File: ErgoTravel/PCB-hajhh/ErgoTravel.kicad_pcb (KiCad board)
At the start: 2 copper layers, 137.9 x 92.7 mm, 43 parts, among them J1 , J10 AudioJack3_Ground, J11 AudioJack3_Ground, J2 , J3 , J4 , J5 , J6 , J7 , J8 , SW1 , SW10 , SW11 , SW12 , SW13 , SW14 , SW15 , SW16 , SW17 , SW18 , SW19 , SW2 , SW20 , SW21 , SW22 , SW23 , SW24 , SW25 , SW26 , SW27 , SW28 , SW29 RST, SW3 , SW30 , SW31 , SW4 , SW5 , SW6 , SW7 , SW8 , SW9 , U1 Promicro

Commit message: update 13:33 24/01/2021
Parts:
- removed the J10 at (200.5, 52.5)
- added D1: , fruitkt:DIODE, F.Cu at (92.7, 64.0)
- added D10: , fruitkt:DIODE, F.Cu at (114.0, 78.5)
- added D11: , fruitkt:DIODE, F.Cu at (152.4, 73.7)
- added D12: , fruitkt:DIODE, F.Cu at (168.9, 74.2)
- added D13: , fruitkt:DIODE, F.Cu at (171.4, 74.2)
- added D14: , fruitkt:DIODE, F.Cu at (190.5, 85.7)
- added D15: , fruitkt:DIODE, F.Cu at (92.7, 102.2)
- added D16: , fruitkt:DIODE, F.Cu at (111.8, 99.6)
- added D17: , fruitkt:DIODE, F.Cu at (130.6, 95.8)
- added D18: , fruitkt:DIODE, F.Cu at (133.4, 95.8)
- added D19: , fruitkt:DIODE, F.Cu at (152.4, 97.8)
- added D2: , fruitkt:DIODE, F.Cu at (111.8, 61.0)
- added D20: , fruitkt:DIODE, F.Cu at (171.4, 99.8)
- added D21: , fruitkt:DIODE, F.Cu at (189.5, 104.1)
- added D22: , fruitkt:DIODE, F.Cu at (92.5, 120.9)
- added D23: , fruitkt:DIODE, F.Cu at (111.5, 117.1)
- added D24: , fruitkt:DIODE, F.Cu at (114.3, 116.8)
- added D25: , fruitkt:DIODE, F.Cu at (133.1, 114.0)
- added D26: , fruitkt:DIODE, F.Cu at (158.1, 116.2)
- added D27: , fruitkt:DIODE, F.Cu at (176.8, 124.5)
- added D28: , fruitkt:DIODE, F.Cu at (179.6, 119.6)
- added D3: , fruitkt:DIODE, F.Cu at (114.3, 60.7)
- added D4: , fruitkt:DIODE, F.Cu at (152.7, 62.0)
- added D5: , fruitkt:DIODE, F.Cu at (168.7, 61.7)
- added D6: , fruitkt:DIODE, F.Cu at (171.2, 61.7)
- added D7: , fruitkt:DIODE, F.Cu at (190.5, 66.3)
- added D8: , fruitkt:DIODE, F.Cu at (93.0, 83.1)
- added D9: , fruitkt:DIODE, F.Cu at (111.5, 78.5)
- added J12: OLED, fruitkt:OLED-0.91, F.Cu at (198.8, 93.4)
- added J13: , fruitkt:USB-C-16pin-hight, F.Cu at (205.8, 52.5)
- added J14: , fruitkt:USB-C-16pin-hight, B.Cu at (205.8, 52.5)
- added J15: , Connector_PinHeader_2.54mm:PinHeader_1x02_P2.54mm_Vertical, F.Cu at (183.1, 114.6)
- added J16: AVR-ISP-6, Connector_PinHeader_2.54mm:PinHeader_2x03_P2.54mm_Vertical, F.Cu at (133.0, 89.0)
- added J3: AudioJack4, Connector_Audio:Jack_3.5mm_PJ320D_Horizontal, F.Cu at (200.5, 52.5)
- added J4: AudioJack4, Connector_Audio:Jack_3.5mm_PJ320D_Horizontal, B.Cu at (200.5, 52.5)
- added JP1: , footprints:Jump, F.Cu at (194.9, 96.3)
- added JP10: , Jumper:SolderJumper-3_P1.3mm_Bridged12_Pad1.0x1.5mm_NumberLabels, F.Cu at (191.5, 53.9)
- added JP2: , footprints:Jump, F.Cu at (197.5, 96.3)
- added JP3: , footprints:Jump, F.Cu at (200.0, 96.3)
- added JP4: , footprints:Jump, F.Cu at (202.6, 96.3)
- added JP5: , footprints:Jump, B.Cu at (194.9, 96.3)
- added JP6: , footprints:Jump, B.Cu at (197.5, 96.3)
- added JP7: , footprints:Jump, B.Cu at (200.0, 96.3)
- added JP8: , footprints:Jump, B.Cu at (202.6, 96.3)
- added JP9: , Jumper:SolderJumper-3_P1.3mm_Bridged12_Pad1.0x1.5mm_NumberLabels, F.Cu at (191.5, 51.3)
- added LED1: , footprints:SK6812mini-e-R2L, F.Cu at (198.8, 66.3)
- added LED10: , footprints:SK6812mini-e-L2R, F.Cu at (160.6, 78.3)
- added LED11: , footprints:SK6812mini-e-L2R, F.Cu at (141.6, 75.9)
- added LED12: , footprints:SK6812mini-e-L2R, F.Cu at (122.5, 78.3)
- added LED13: , footprints:SK6812mini-e-L2R, F.Cu at (103.5, 80.7)
- added LED14: , footprints:SK6812mini-e-L2R, F.Cu at (84.4, 83.1)
- added LED15: , footprints:SK6812mini-e-R2L, F.Cu at (179.7, 99.7)
- added LED16: , footprints:SK6812mini-e-R2L, F.Cu at (160.6, 97.3)
- added LED17: , footprints:SK6812mini-e-R2L, F.Cu at (141.6, 95.0)
- added LED18: , footprints:SK6812mini-e-R2L, F.Cu at (122.5, 97.3)
- added LED19: , footprints:SK6812mini-e-R2L, F.Cu at (103.5, 99.7)
- added LED2: , footprints:SK6812mini-e-R2L, F.Cu at (179.7, 61.6)
- added LED20: , footprints:SK6812mini-e-R2L, F.Cu at (84.4, 102.1)
- added LED21: , footprints:SK6812mini-e-L2R, F.Cu at (84.4, 121.1)
- added LED22: , footprints:SK6812mini-e-L2R, F.Cu at (200.0, 109.7)
- added LED23: , footprints:SK6812mini-e-R2L, F.Cu at (195.2, 117.9)
- added LED24: , footprints:SK6812mini-e-L2R, F.Cu at (167.2, 118.4)
- added LED25: , footprints:SK6812mini-e-L2R, F.Cu at (141.6, 114.0)
- added LED26: , footprints:SK6812mini-e-L2R, F.Cu at (122.6, 116.4)
- added LED27: , footprints:SK6812mini-e-L2R, F.Cu at (103.5, 118.8)
- added LED28: , fruitkt:SK6812MINI-FLIP, F.Cu at (170.1, 68.8)
- added LED29: , fruitkt:SK6812MINI-FLIP, F.Cu at (170.2, 88.7)
- added LED3: , footprints:SK6812mini-e-R2L, F.Cu at (160.6, 59.2)
- added LED30: , fruitkt:SK6812MINI-FLIP, F.Cu at (170.2, 109.2)
- added LED31: , fruitkt:SK6812MINI-FLIP, F.Cu at (113.0, 109.2)
- added LED32: , fruitkt:SK6812MINI-FLIP, F.Cu at (113.0, 88.6)
- added LED33: , fruitkt:SK6812MINI-FLIP, F.Cu at (113.0, 69.1)
- added LED4: , footprints:SK6812mini-e-R2L, F.Cu at (141.7, 56.8)
- added LED5: , footprints:SK6812mini-e-R2L, F.Cu at (122.5, 59.1)
- added LED6: , footprints:SK6812mini-e-R2L, F.Cu at (103.5, 61.6)
- added LED7: , footprints:SK6812mini-e-R2L, F.Cu at (84.4, 63.9)
- added LED8: , footprints:SK6812mini-e-L2R, F.Cu at (198.7, 85.4)
- added LED9: , footprints:SK6812mini-e-L2R, F.Cu at (179.7, 80.7)
- added R1: 4K7, Resistor_SMD:R_0805_2012Metric, F.Cu at (186.4, 53.9)
- added R2: 4K7, Resistor_SMD:R_0805_2012Metric, F.Cu at (186.4, 51.2)
- J11: value AudioJack3_Ground -> (none); footprint Connector_Audio:Jack_3.5mm_PJ320D_Horizontal -> Connector_PinHeader_2.54mm:PinHeader_1x02_P2.54mm_Vertical; moved to F.Cu
- SW16: renamed from SW29; footprint Button_Switch_SMD:SW_SPST_TL3342 -> footprints:SW_TACT_ALPS_SKQGABE010
- SW8: renamed from SW30; footprint Button_Switch_SMD:SW_SPDT_PCM12 -> footprints:SW_SPDT_PCM12
- moved J11 80.6 mm to (120.0, 49.0)
- moved SW8 5.90 mm to (127.6, 49.3), turned to 0 degrees
- moved SW16 1.45 mm to (111.9, 51.2), turned to 10 degrees
- moved U1 0.25 mm to (141.6, 64.3)
- renumbered J8 to J10, J5 to J2, J2 to J5, J3 to J7, J7 to J8, J4 to J9, SW6 to SW10, SW10 to SW11, SW14 to SW12, SW18 to SW13, SW22 to SW14, SW27 to SW15, SW25 to SW17, SW31 to SW18, SW3 to SW19, SW5 to SW2, SW7 to SW20, SW11 to SW21, SW15 to SW22, SW19 to SW23, SW23 to SW24, SW28 to SW25, SW4 to SW26, SW8 to SW27, SW12 to SW28, SW16 to SW29, SW9 to SW3, SW20 to SW30, SW24 to SW31, SW13 to SW4, SW17 to SW5, SW21 to SW6, SW26 to SW7, SW2 to SW9
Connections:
- net Net-(SW29-Pad1) renamed RST
- net Net-(U1-PadB5) renamed backlight
- SW1 pad 1: Net-(SW1-Pad1) -> col0
- SW10 pad 1: Net-(SW6-Pad1) -> col1
- SW11 pad 1: Net-(SW10-Pad1) -> col2
- SW12 pad 1: Net-(SW14-Pad1) -> col3
- SW13 pad 1: Net-(SW18-Pad1) -> col4
- SW14 pad 1: Net-(SW22-Pad1) -> col5
- SW15 pad 1: Net-(SW27-Pad1) -> col6
- SW17 pad 1: Net-(D27-Pad2) (its old number) -> col6
- SW17 pad 2: Net-(SW25-Pad2) -> Net-(D21-Pad2)
- SW18 pad A: Net-(SW31-PadA) -> A
- SW18 pad B: Net-(SW31-PadB) -> B
- SW18 pad S1: Net-(SW31-PadS1) -> col6
- SW18 pad S2: Net-(SW31-PadS2) -> Net-(D21-Pad2)
- SW19 pad 1: Net-(SW3-Pad1) -> col0
- SW2 pad 1: Net-(SW5-Pad1) -> col1
- SW20 pad 1: Net-(SW7-Pad1) -> col1
- SW21 pad 1: Net-(SW11-Pad1) -> col2
- SW22 pad 1: Net-(SW15-Pad1) -> col3
- SW23 pad 1: Net-(SW19-Pad1) -> col4
- SW24 pad 1: Net-(SW23-Pad1) -> col5
- SW25 pad 1: Net-(SW25-Pad2) -> Net-(D21-Pad2)
- SW25 pad 2: Net-(D27-Pad2) (its old number) -> col6
- SW26 pad 1: Net-(SW4-Pad1) -> col0
- SW27 pad 1: Net-(SW8-Pad1) (its old number) -> col1
- SW28 pad 1: Net-(SW12-Pad1) -> col2
- SW29 pad 1: Net-(SW16-Pad1) -> col3
- SW3 pad 1: Net-(SW9-Pad1) -> col2
- SW30 pad 1: Net-(SW20-Pad1) -> col4
- SW31 pad 1: Net-(SW24-Pad1) -> col5
- SW4 pad 1: Net-(SW13-Pad1) -> col3
- SW5 pad 1: Net-(SW17-Pad1) -> col4
- SW6 pad 1: Net-(SW21-Pad1) -> col5
- SW7 pad 1: Net-(SW26-Pad1) -> col6
- SW8 pad 3: Net-(SW30-Pad3) -> Net-(J11-Pad1)
- SW9 pad 1: Net-(SW2-Pad1) -> col0
- U1 pad B1: Net-(U1-PadB1) -> col3
- U1 pad B2: Net-(U1-PadB2) -> col5
- U1 pad B3: Net-(U1-PadB3) -> col4
- U1 pad B4: Net-(U1-PadB4) -> row3
- U1 pad B6: Net-(U1-PadB6) -> col6
- U1 pad C6: Net-(U1-PadC6) -> row0
- U1 pad D0: Net-(U1-PadD0) -> scl
- U1 pad D1: Net-(U1-PadD1) -> sda
- U1 pad D2: Net-(U1-PadD2) -> rx
- U1 pad D3: Net-(U1-PadD3) -> led
- U1 pad D4: Net-(U1-PadD4) -> A
- U1 pad D7: Net-(U1-PadD7) -> row1
- U1 pad E6: Net-(U1-PadE6) -> row2
- U1 pad F4: Net-(U1-PadF4) -> B
- U1 pad F5: Net-(U1-PadF5) -> col0
- U1 pad F6: Net-(U1-PadF6) -> col1
- U1 pad F7: Net-(U1-PadF7) -> col2
- U1 pad VCC: Net-(U1-PadVCC) -> VCC
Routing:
- net VCC: track 0.00 -> 988.8 mm, vias 0 -> 20
- net GND: track 0.00 -> 528.7 mm, vias 0 -> 21
- net col6: track 0.00 -> 172.5 mm
- net col5: track 0.00 -> 168.0 mm
- net row3: track 0.00 -> 145.7 mm
- net col0: track 0.00 -> 143.1 mm
- net col4: track 0.00 -> 140.4 mm
- net row2: track 0.00 -> 131.7 mm
- net col1: track 0.00 -> 125.4 mm
- net row1: track 0.00 -> 122.5 mm, vias 0 -> 1
- net col3: track 0.00 -> 121.1 mm
- net row0: track 0.00 -> 113.5 mm
- net scl: track 0.00 -> 110.3 mm, vias 0 -> 1
- net sda: track 0.00 -> 105.2 mm, vias 0 -> 2
- net col2: track 0.00 -> 103.2 mm
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- added copper zone on B.Cu, net GND
- added copper zone on F.Cu, net GND
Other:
- net class Wires: trace_width 0.5 -> 0.4
- board text added: "Use ProMicro or nRFMicro"
- board text removed: "Extra Key"
- board text removed: "Install D28 for Extra Key"
- board text removed: "Use Pro Micro or BlueMicro"

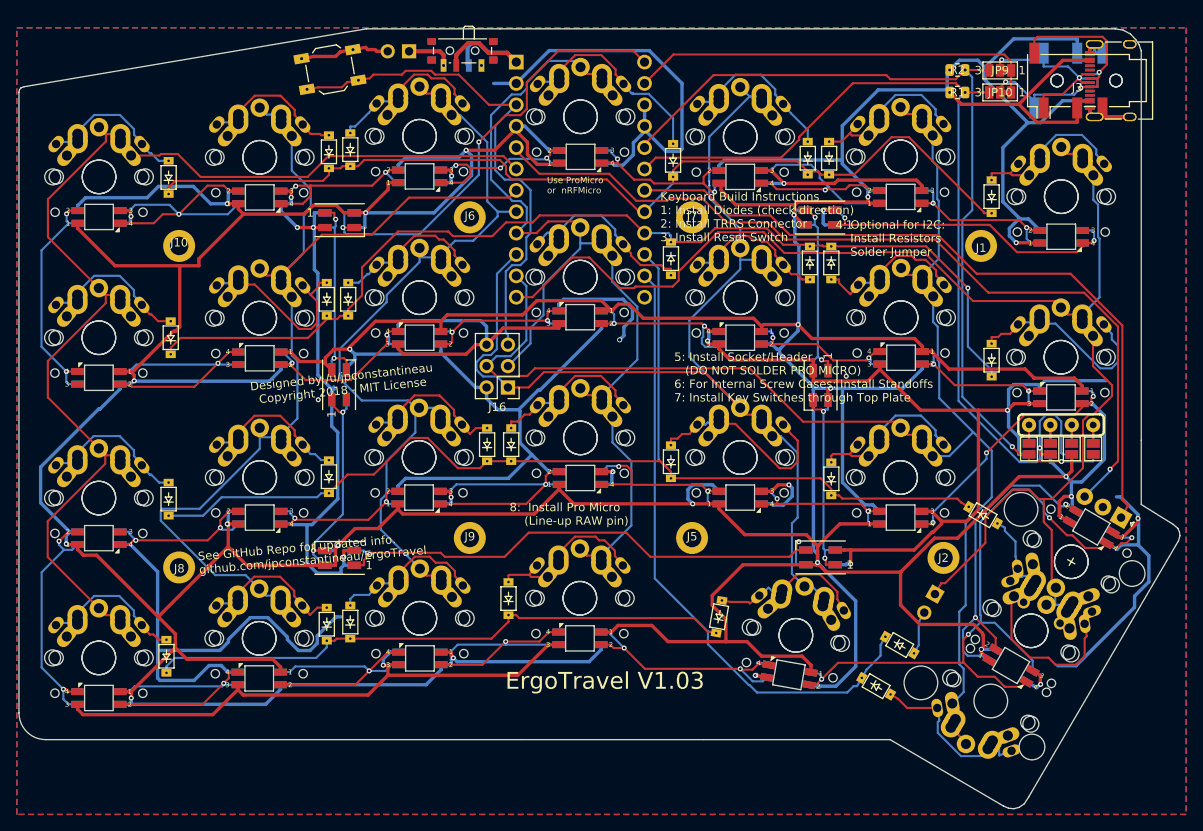
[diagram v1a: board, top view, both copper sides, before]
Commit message: add some keyboard
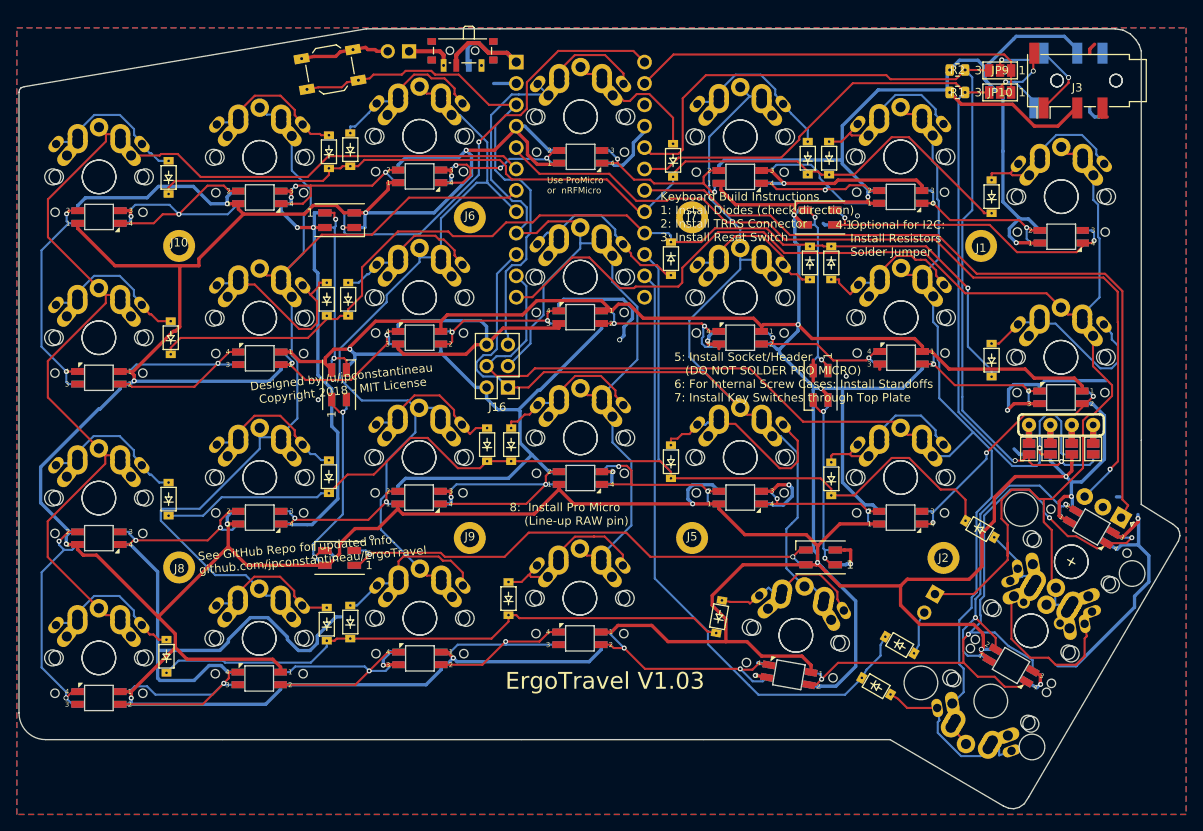
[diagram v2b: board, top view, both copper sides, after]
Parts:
- removed J13, J14: , fruitkt:USB-C-16pin-hight
- moved D21 1.69 mm to (189.1, 105.8)
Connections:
- J1 pad 1: Net-(J1-Pad1) -> GND
- J10 pad 1: Net-(J10-Pad1) -> GND
- J2 pad 1: Net-(J2-Pad1) -> GND
- J5 pad 1: Net-(J5-Pad1) -> GND
- J6 pad 1: Net-(J6-Pad1) -> GND
- J7 pad 1: Net-(J7-Pad1) -> GND
- J8 pad 1: Net-(J8-Pad1) -> GND
- J9 pad 1: Net-(J9-Pad1) -> GND
- SW4 pad 1: col3 -> Net-(D4-Pad2)
- SW4 pad 2: Net-(D4-Pad2) -> col3
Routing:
- net GND: track 528.7 -> 318.9 mm
- net VCC: track 988.8 -> 963.3 mm
- net 1: track 35.6 -> 11.6 mm, vias 3 -> 2
- net 2: track 26.4 -> 16.1 mm
- net Net-(D4-Pad2): track 26.9 -> 18.0 mm
- net sda: track 105.2 -> 111.4 mm
- net row2: track 131.7 -> 137.2 mm
- net col6: track 172.5 -> 177.6 mm
- net col3: track 121.1 -> 125.9 mm
- net Net-(LED30-PadI): track 64.7 -> 61.2 mm
- net B: track 102.6 -> 105.0 mm
- net A: track 86.8 -> 89.2 mm
- net Net-(LED31-PadI): track 25.6 -> 27.4 mm
- net Net-(D21-Pad2): track 38.7 -> 37.2 mm
- net scl: track 110.3 -> 111.7 mm
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
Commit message: cap nhat 12:00 18/03/2021
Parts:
- moved D23 0.47 mm to (111.9, 116.9)
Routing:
- net GND: track 318.9 -> 256.9 mm, vias 21 -> 20
- net VCC: track 963.3 -> 971.6 mm
- net row1: track 122.5 -> 127.2 mm
- net row3: track 145.4 -> 149.0 mm
- net Net-(LED26-PadI): track 30.6 -> 32.6 mm
- net Net-(LED24-PadI): track 29.0 -> 28.0 mm
- net Net-(D7-Pad2): track 20.4 -> 19.5 mm
- net Net-(LED30-PadI): track 61.2 -> 62.0 mm
- net Net-(D17-Pad2): track 20.1 -> 19.5 mm
- net col6: track 177.6 -> 178.2 mm
- net Net-(D27-Pad2): track 23.2 -> 23.7 mm
- net Net-(D18-Pad2): track 21.1 -> 20.6 mm
- net Net-(D19-Pad2): track 27.3 -> 26.7 mm
- added copper zone on B.Cu, net (none)
- added copper zone on F.Cu, net (none)
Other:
- board text added: "Bat+"
- board text added: "GND"
- board text added: "Raw"
- board text removed: "4: Optional for I2C: Install Resistors Solder Jumper"
- board text removed: "5: Install Socket/Header (DO NOT SOLDER PRO MICRO) 6: For Internal Screw Cases: Install Standoffs 7: Install Key Switches through Top Plate"
- board text removed: "8: Install Pro Micro (Line-up RAW pin)"
- board text removed: "Designed by /u/jpconstantineau Copyright 2018 - MIT License"
- board text removed: "Keyboard Build Instructions 1: Install Diodes (check direction) 2: Install TRRS Connector 3: Install Reset Switch"
- board text removed: "See GitHub Repo for updated info. github.com/jpconstantineau/ErgoTravel"
